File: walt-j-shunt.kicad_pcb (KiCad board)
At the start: 2 copper layers, 70 x 50 mm, 59 parts, among them J1 Screw_Terminal_01x03, Q1 NMOS, Q2 NJVMJD45H11T4G, Q3 PNP, Q4 NMOS, Q5 NJVMJD45H11T4G, Q6 PNP, U1 AD817, U2 AD817

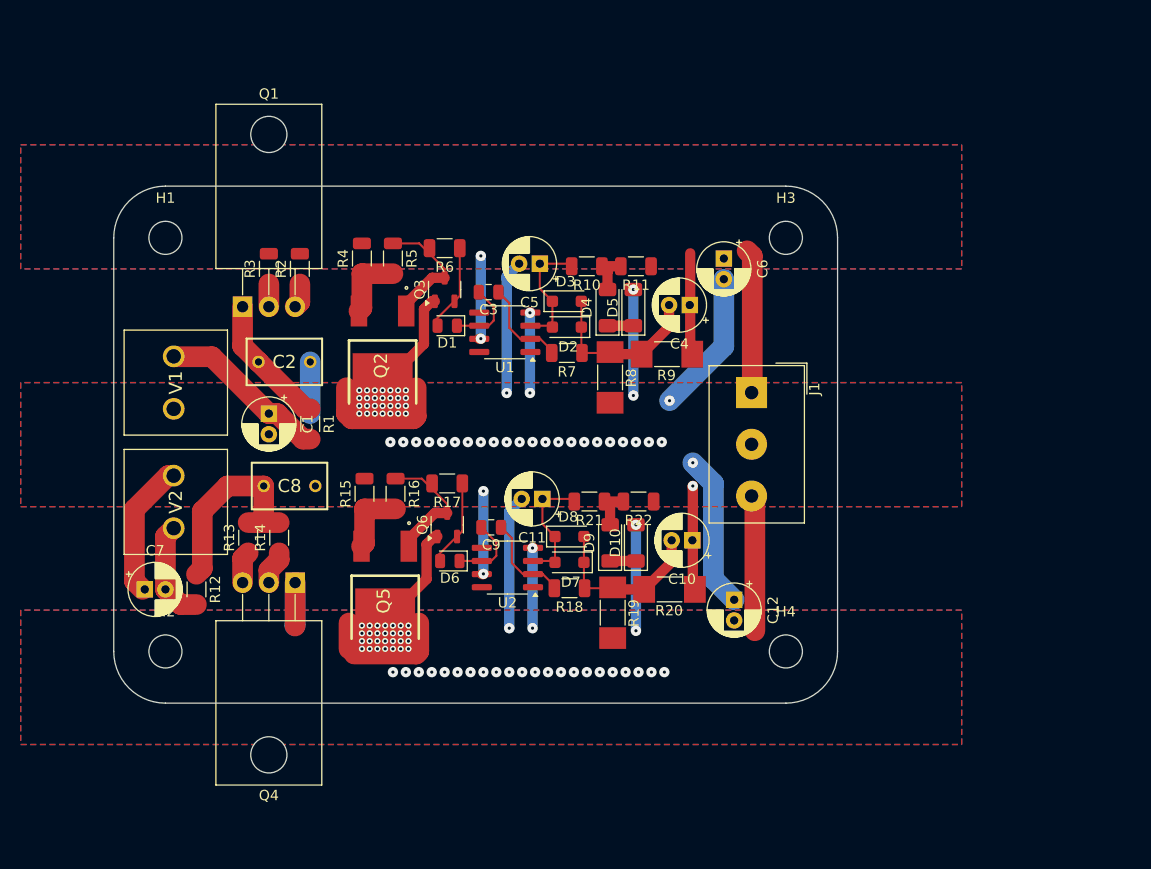
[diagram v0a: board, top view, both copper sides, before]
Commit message: Current design with SMD MOSFET (before switching to THT)
🤖 Generated with [Claude Code](https://claude.ai/code)

Co-Authored-By: Claude <noreply@anthropic.com>
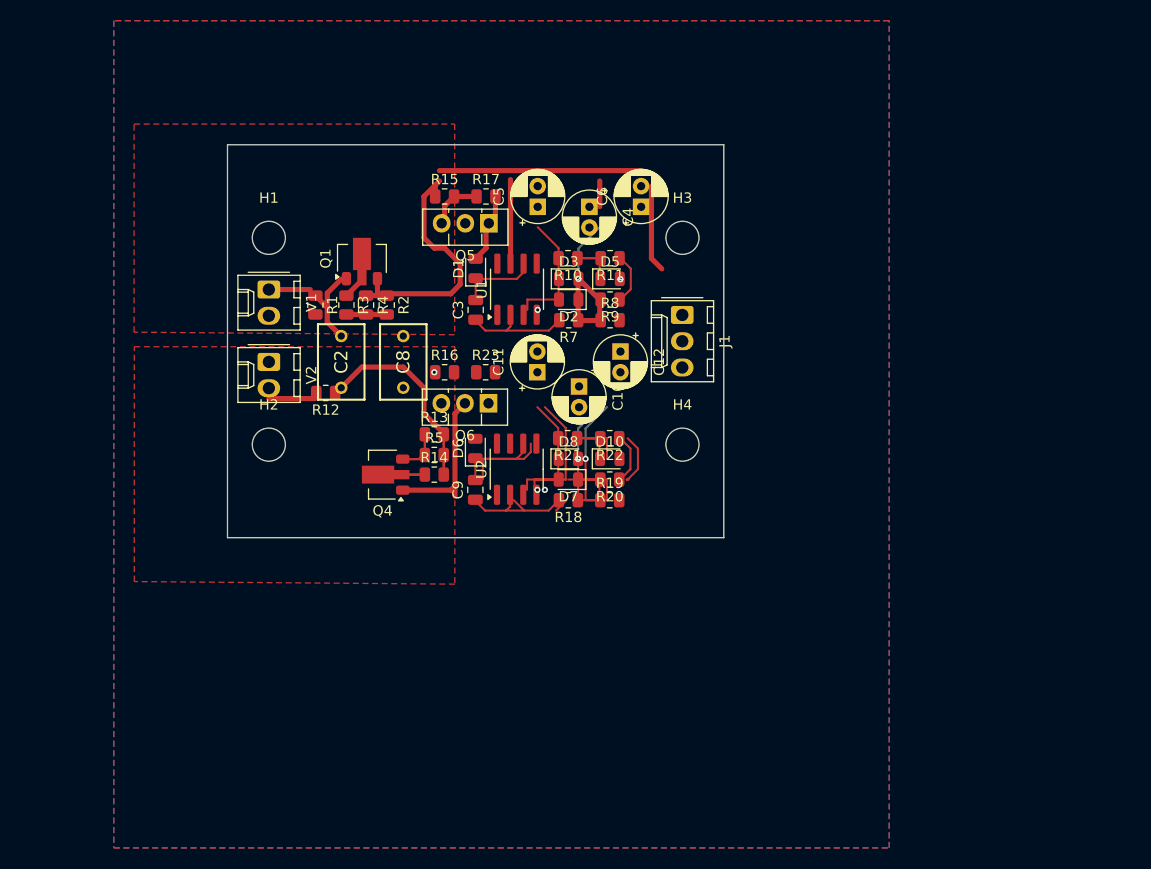
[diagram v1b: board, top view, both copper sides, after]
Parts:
- removed C1, C7: 120u, Capacitor_THT:CP_Radial_D5.0mm_P2.00mm
- removed D4, D9: D_Zener, Diode_SMD:D_MiniMELF
- removed Q2: NJVMJD45H11T4G, Samacsys:DPAK_(SINGLE-GAUGE)_TO-252(369C)_ISSUE_F
- removed Q3: PNP, Package_TO_SOT_SMD:SOT-23-3
- removed R6: 221r, Resistor_SMD:R_1206_3216Metric
- added R23: 440r, Resistor_SMD:R_0805_2012Metric, F.Cu at (131.0, 73.0)
- D10, D5: footprint Diode_SMD:D_MiniMELF -> Diode_SMD:D_0805_2012Metric
- D2, D3, D7, D8: footprint Diode_SMD:D_SOD-123F -> Diode_SMD:D_0805_2012Metric
- J1: footprint TerminalBlock_Altech:Altech_AK100_1x03_P5.00mm -> Connector_Molex:Molex_KK-254_AE-6410-03A_1x03_P2.54mm_Vertical
- Q1, Q4: footprint Package_TO_SOT_THT:TO-220-3_Horizontal_TabDown -> Package_TO_SOT_SMD:SOT-89-3
- Q5: value NJVMJD45H11T4G -> BD680; footprint Samacsys:DPAK_(SINGLE-GAUGE)_TO-252(369C)_ISSUE_F -> Package_TO_SOT_THT:TO-126-3_Vertical
- Q6: value PNP -> BD680; footprint Package_TO_SOT_SMD:SOT-23-3 -> Package_TO_SOT_THT:TO-126-3_Vertical
- R1, R10, R11, R12, R14, R15, R18, R21, R22, R3, R7: footprint Resistor_SMD:R_1206_3216Metric -> Resistor_SMD:R_0805_2012Metric
- R13, R2: value 5r -> 20r; footprint Resistor_SMD:R_1206_3216Metric -> Resistor_SMD:R_0805_2012Metric
- R16: value 49.9r -> 1r; footprint Resistor_SMD:R_1206_3216Metric -> Resistor_SMD:R_0805_2012Metric
- R17: value 221r -> 440r; footprint Resistor_SMD:R_1206_3216Metric -> Resistor_SMD:R_0805_2012Metric
- R19, R20, R8, R9: footprint Resistor_SMD:R_MELF_MMB-0207 -> Resistor_SMD:R_0805_2012Metric
- R4: value 1r -> 20r; footprint Resistor_SMD:R_1206_3216Metric -> Resistor_SMD:R_0805_2012Metric
- R5: value 49.9r -> 20r; footprint Resistor_SMD:R_1206_3216Metric -> Resistor_SMD:R_0805_2012Metric
- V1, V2: footprint Samacsys:395443002 -> Connector_Molex:Molex_KK-254_AE-6410-02A_1x02_P2.54mm_Vertical
- moved Q5 41.4 mm to (131.3, 58.6), turned to 180 degrees
- moved R15 29.8 mm to (127.0, 56.0), turned to 0 degrees
- moved Q4 29.2 mm to (121.0, 82.9)
- moved R17 28.0 mm to (131.0, 56.0), turned to 0 degrees
- moved C12 26.4 mm to (144.0, 71.0)
- moved R12 22.7 mm to (115.5, 75.0), turned to 180 degrees
- moved H2 22.4 mm to (110.0, 80.0)
- moved H4 22.4 mm to (150.0, 80.0)
- moved R13 20.6 mm to (126.0, 79.0), turned to 0 degrees
- moved R5 19.4 mm to (126.0, 81.0), turned to 0 degrees
- moved C10 18.5 mm to (140.0, 74.4), turned to -90 degrees
- moved C8 16.8 mm to (123.0, 69.5), turned to -90 degrees
- moved R14 16.2 mm to (126.0, 82.9), turned to 0 degrees
- moved Q1 15.0 mm to (119.0, 62.0), turned to 90 degrees
- moved V2 14.3 mm to (110.0, 72.0)
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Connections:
- net Net-(Q1-G) renamed /current_source/m_g
- net Net-(Q4-G) renamed /current_source1/m_g
- D5 pad 1: Net-(D4-K) -> Net-(D5-K)
- Q5 pad 1: Net-(Q6-E) -> Net-(D1-A)
- Q5 pad 2: Net-(Q5-Pad2) -> GND
- Q5 pad 3: neg_reg_out -> Net-(Q5-E)
- Q6 pad 1: neg_reg_out -> Net-(D6-A)
- Q6 pad 2: Net-(D6-A) -> neg_reg_out
- R10 pad 1: Net-(D4-A) -> Net-(D5-K)
- R11 pad 2: Net-(D4-A) -> Net-(D5-K)
- R15 pad 1: Net-(Q5-Pad2) -> pos_reg_out
- R15 pad 2: GND -> Net-(Q5-E)
- R16 pad 1: Net-(Q6-E) -> GND
- R16 pad 2: Net-(Q5-Pad2) -> Net-(Q6-E)
- R17 pad 1: Net-(D6-A) -> Net-(Q5-E)
- R17 pad 2: Net-(Q6-E) -> Net-(D1-A)
- R21 pad 1: Net-(D9-A) -> Net-(D10-K)
- R22 pad 2: Net-(D9-A) -> Net-(D10-K)
- R4 pad 1: Net-(Q2-Pad2) -> Net-(Q1-S)
- R5 pad 1: Net-(Q3-E) -> Net-(Q4-S)
- R5 pad 2: Net-(Q2-Pad2) -> /current_source1/plus
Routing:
- net GND: track 121.6 -> 10.2 mm, vias 60 -> 3
- net neg_reg_out: track 76.6 -> 14.6 mm, vias 55 -> 2
- net pos_reg_out: track 32.1 -> 68.9 mm, vias 2 -> 0
- net Net-(D7-K): track 17.2 -> 33.9 mm, vias 0 -> 2
- net Net-(Q6-E): track 12.3 -> 0.00 mm
- net Net-(Q3-E): track 12.3 -> 0.00 mm
- net bank-plus: track 16.5 -> 4.71 mm
- net Net-(D7-A): track 12.1 -> 23.8 mm
- net Net-(D10-K): track 2.50 -> 12.2 mm
- net Net-(D6-K): track 7.37 -> 15.5 mm
- net Net-(D6-A): track 8.01 -> 0.00 mm
- net Net-(Q2-Pad2): track 6.73 -> 0.00 mm
- net Net-(Q5-Pad2): track 6.73 -> 0.00 mm
- net Net-(D5-K): track 0.00 -> 6.09 mm
- net Net-(Q4-S): track 3.10 -> 8.79 mm
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- added copper zone on F.Cu, net /current_source/m_g
- added copper zone on F.Cu, net /current_source1/m_g
- removed copper zone on B.Cu, net neg_reg_out
- removed copper zone on F.Cu, net neg_reg_out
- removed copper zone on B.Cu, net pos_reg_out
- removed copper zone on F.Cu, net pos_reg_out
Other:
- board size 70 x 50 mm -> 48 x 38 mm

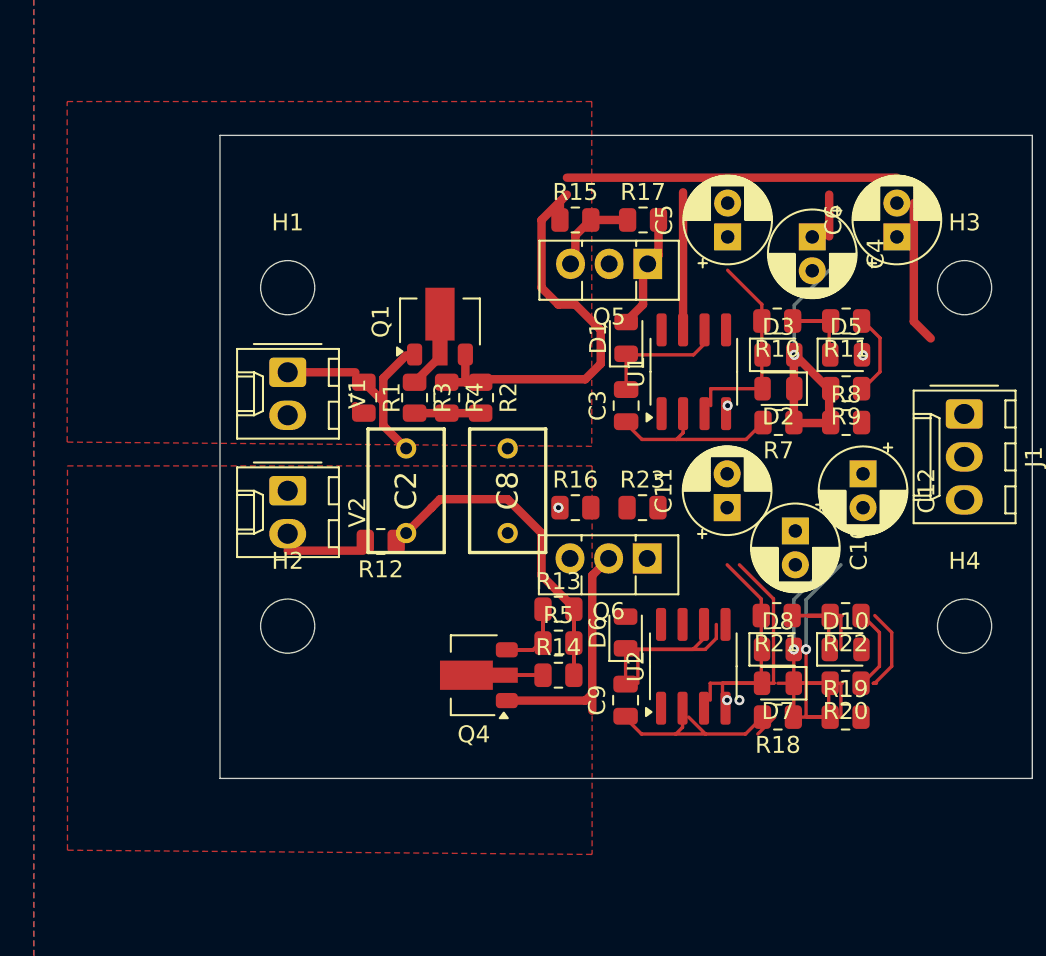
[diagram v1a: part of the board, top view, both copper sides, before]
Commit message: Switch to THT MOSFET - need to verify pinout, rough but closer
🤖 Generated with [Claude Code](https://claude.ai/code)

Co-Authored-By: Claude <noreply@anthropic.com>
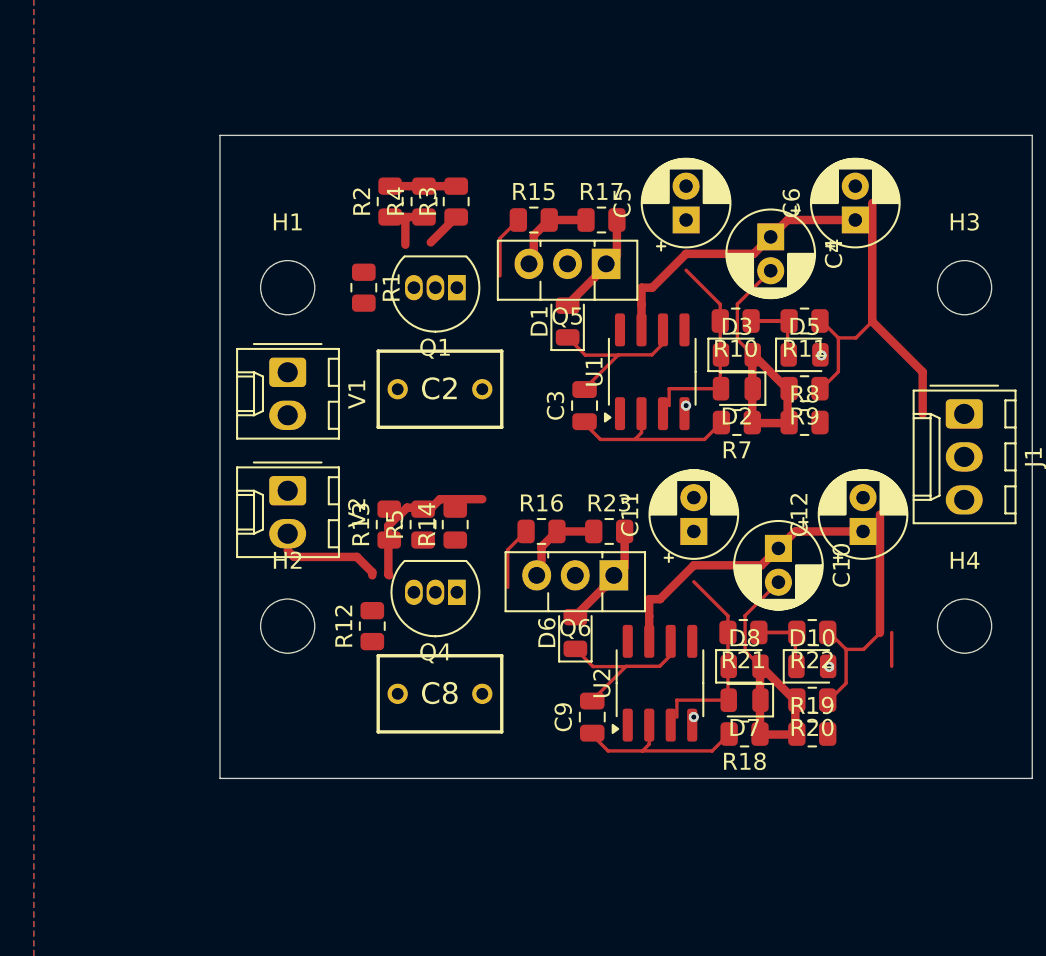
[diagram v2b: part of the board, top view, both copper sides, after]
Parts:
- Q1, Q4: footprint Package_TO_SOT_SMD:SOT-89-3 -> Package_TO_SOT_THT:TO-92_Inline
- moved C8 14.6 mm to (121.5, 84.0), turned to 180 degrees
- moved R2 12.8 mm to (116.1, 54.9), turned to 90 degrees
- moved R3 11.8 mm to (120.0, 54.9), turned to 90 degrees
- moved R4 11.7 mm to (118.1, 54.9), turned to 90 degrees
- moved R13 11.2 mm to (116.0, 74.0), turned to 90 degrees
- moved R14 10.8 mm to (119.9, 74.0), turned to 90 degrees
- moved R5 10.6 mm to (118.0, 74.0), turned to 90 degrees
- moved R1 6.50 mm to (114.5, 60.0)
- moved R12 5.02 mm to (115.0, 80.0), turned to 90 degrees
- moved Q4 5.00 mm to (120.0, 78.0)
- moved D1 3.59 mm to (126.5, 62.0)
- moved C2 3.54 mm to (116.5, 66.0), turned to 0 degrees
- moved C12 3.41 mm to (144.0, 74.4), turned to 90 degrees
- moved D6 2.97 mm to (127.0, 80.4)
- moved C5 2.65 mm to (133.5, 56.0)
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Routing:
- net GND: track 10.2 -> 37.0 mm, vias 3 -> 2
- net pos_reg_out: track 68.9 -> 45.8 mm
- net Net-(D7-K): track 33.9 -> 17.1 mm, vias 2 -> 0
- net /current_source1/plus: track 23.8 -> 9.16 mm
- net neg_reg_out: track 14.6 -> 0.00 mm
- net Net-(D7-A): track 23.8 -> 11.9 mm
- net Net-(Q4-S): track 8.79 -> 0.00 mm
- net pre-cur: track 8.25 -> 0.00 mm
- net Net-(D6-A): track 0.00 -> 6.21 mm
- net /current_source1/m_g: track 6.18 -> 0.00 mm
- net Net-(D10-K): track 12.2 -> 6.09 mm
- net Net-(D6-K): track 15.5 -> 9.97 mm
- net Net-(Q6-E): track 0.00 -> 5.47 mm
- net bank-plus: track 4.71 -> 0.00 mm
- net Net-(U2--): track 13.5 -> 10.6 mm
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- removed copper zone on F.Cu, net /current_source/m_g
- removed copper zone on F.Cu, net /current_source1/m_g

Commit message: Half layout done
🤖 Generated with [Claude Code](https://claude.ai/code)

Co-Authored-By: Claude <noreply@anthropic.com>
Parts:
- removed C11, C12: 120u, Capacitor_THT:CP_Radial_D5.0mm_P2.00mm
- removed D10: D_Zener, Diode_SMD:D_0805_2012Metric
- removed the R12 at (115.0, 80.0)
- removed the R14 at (119.9, 74.0)
- removed the R5 at (118.0, 74.0)
- added C7: 33pf, Capacitor_SMD:C_0805_2012Metric, F.Cu at (166.6, 96.9)
- added D4: gled, LED_SMD:LED_0805_2012Metric, F.Cu at (145.5, 55.5)
- added Q2: D45H11G, Package_TO_SOT_THT:TO-220-3_Vertical, F.Cu at (134.5, 55.1)
- added Q3: MMBT2907AL, Package_TO_SOT_SMD:SOT-23-3, F.Cu at (131.0, 58.5)
- added Q7: MMBT2907AL, Package_TO_SOT_SMD:SOT-23-3, F.Cu at (160.3, 96.4)
- added Q8: ZTX951, Package_TO_SOT_THT:TO-92Flat, F.Cu at (170.3, 97.2)
- added R15: 20r, Resistor_SMD:R_0805_2012Metric, F.Cu at (184.6, 81.8)
- added R17: 100r, Resistor_SMD:R_0805_2012Metric, F.Cu at (184.6, 87.7)
- added R24: 1k, Resistor_SMD:R_0805_2012Metric, F.Cu at (175.4, 75.8)
- added R25: 150r, Resistor_SMD:R_0805_2012Metric, F.Cu at (175.4, 78.8)
- added R26: 1.8k, Resistor_SMD:R_0805_2012Metric, F.Cu at (175.4, 81.7)
- added R3: 20r, Resistor_SMD:R_0805_2012Metric, F.Cu at (116.5, 58.5)
- added R7: 50r, Resistor_SMD:R_0805_2012Metric, F.Cu at (127.0, 58.5)
- added V2: VSIN, Connector_Molex:Molex_KK-254_AE-6410-02A_1x02_P2.54mm_Vertical, F.Cu at (184.7, 95.1)
- C10, C4, C5, C6: value 120u -> 100uf
- C8: value 1uf -> 100uf; footprint Samacsys:B32529C105J -> Capacitor_THT:CP_Radial_D5.0mm_P2.00mm
- C9: value 33pf -> 100uf; footprint Capacitor_SMD:C_0805_2012Metric -> Capacitor_THT:CP_Radial_D5.0mm_P2.00mm
- D1: value LED -> rled
- D5: value D_Zener -> rled
- D6: value LED -> D
- D8: value D -> gled; footprint Diode_SMD:D_0805_2012Metric -> LED_SMD:LED_0805_2012Metric
- Q1: value NMOS -> DN2540; footprint Package_TO_SOT_THT:TO-92_Inline -> Package_TO_SOT_THT:TO-220-3_Vertical
- Q4: value NMOS -> ZTX951; footprint Package_TO_SOT_THT:TO-92_Inline -> Package_TO_SOT_THT:TO-92Flat
- Q5: value BD680 -> DN2540; footprint Package_TO_SOT_THT:TO-126-3_Vertical -> Package_TO_SOT_THT:TO-220-3_Vertical
- Q6: value BD680 -> D45H11G; footprint Package_TO_SOT_THT:TO-126-3_Vertical -> Package_TO_SOT_THT:TO-220-3_Vertical
- R10: renamed from R8; value 1k -> 500r
- R11: renamed from R9; value 800r -> 2k
- R13: value 20r -> 150r
- R14: renamed from R11; value 1.82k -> 1.8k
- R16: value 1r -> 20r
- R18: value 499 -> 1r
- R19: value 1k -> 50r
- R2: value 20r -> 1r
- R20: value 800r -> 221r
- R21: value 1k -> 475
- R22: value 1.82k -> 500r
- R23: value 440r -> 2k
- R8: renamed from R17; value 440r -> 221r
- R9: renamed from R7; value 499 -> 475
- moved R2 82.3 mm to (184.6, 100.5), turned to 0 degrees
- moved R16 60.5 mm to (184.6, 84.8)
- moved Q5 60.1 mm to (185.6, 78.3), turned to 0 degrees
- moved R23 42.6 mm to (171.0, 81.7)
- moved U2 42.1 mm to (173.1, 92.5), turned to 0 degrees
- moved D6 40.3 mm to (166.6, 87.8), turned to 0 degrees
- moved C8 39.1 mm to (160.1, 77.6), turned to 0 degrees
- moved R21 34.4 mm to (171.0, 75.8), turned to 0 degrees
- moved D5 33.3 mm to (166.6, 84.7)
- moved R13 33.2 mm to (143.5, 55.5)
- moved Q4 32.2 mm to (141.2, 53.7), turned to -90 degrees
- moved C9 32.1 mm to (160.1, 84.2), turned to 0 degrees
- moved D8 31.8 mm to (166.6, 93.9)
- moved R18 31.4 mm to (166.6, 75.8), turned to 0 degrees
- moved D7 30.3 mm to (166.6, 90.8), turned to 0 degrees
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- renumbered C2 to C1, R10 to R12, R3 to R5, R15 to R6
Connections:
- C10 pad 2: Net-(D7-K) -> neg_reg_out
- C8 pad 2: /current_source1/plus -> Net-(D6-K)
- C9 pad 1: Net-(U2--) -> Net-(D6-A)
- C9 pad 2: Net-(D6-K) -> neg_reg_out
- D5 pad 2: GND -> Net-(D5-A)
- D7 pad 1: Net-(D7-K) -> Net-(D6-A)
- D7 pad 2: Net-(D7-A) -> Net-(D6-K)
- D8 pad 1: Net-(D7-A) -> neg_reg_out
- D8 pad 2: Net-(D7-K) -> Net-(D8-A)
- Q4 pad 1: neg_reg_out -> GND
- Q4 pad 2: /current_source1/m_g -> Net-(D4-A)
- Q4 pad 3: Net-(Q4-S) -> /reg/v-ref
- Q5 pad 1: Net-(D1-A) -> neg_reg_out
- Q5 pad 2: GND -> /current_source1/m_g
- Q5 pad 3: Net-(Q5-E) -> Net-(Q5-S)
- Q6 pad 1: Net-(D6-A) -> Net-(Q6-B)
- R12 pad 1: Net-(D5-K) -> /reg/v-ref
- R13 pad 1: Net-(Q4-S) -> /reg/v-ref
- R13 pad 2: /current_source1/plus -> Net-(D4-A)
- R14 pad 2: Net-(D5-K) -> /reg/v-ref
- R16 pad 1: GND -> Net-(Q5-S)
- R16 pad 2: Net-(Q6-E) -> /current_source1/+
- R18 pad 1: Net-(D7-K) -> GND
- R18 pad 2: Net-(U2--) -> Net-(Q6-E)
- R19 pad 1: Net-(D7-K) -> Net-(Q6-E)
- R19 pad 2: neg_reg_out -> Net-(Q6-B)
- R2 pad 1: Net-(Q1-S) -> /current_source1/+
- R2 pad 2: pos_reg_out -> Net-(R2-Pad2)
- R20 pad 1: GND -> Net-(Q6-B)
- R20 pad 2: Net-(D7-K) -> Net-(D5-A)
- R21 pad 1: Net-(D10-K) -> Net-(D6-K)
- R21 pad 2: Net-(D7-A) -> Net-(U2--)
- R22 pad 1: GND -> Net-(D6-K)
- R22 pad 2: Net-(D10-K) -> neg_reg_out
- R23 pad 1: Net-(Q6-E) -> GND
- R23 pad 2: Net-(D6-A) -> Net-(D6-K)
- R6 pad 2: Net-(Q5-E) -> Net-(Q2-E)
- R8 pad 1: Net-(Q5-E) -> Net-(Q2-B)
- U1 pad 1: unconnected-(U1-NULL-Pad1) -> Net-(D2-A)
- U1 pad 3: Net-(D2-A) -> pos_reg_out
- U1 pad 5: unconnected-(U1-NC-Pad5) -> Net-(D1-K)
- U1 pad 6: Net-(D1-K) -> (no net)
- U1 pad 7: pos_reg_out -> (no net)
- U1 pad 8: unconnected-(U1-NULL-Pad8) -> (no net)
- U2 pad 1: unconnected-(U2-NULL-Pad1) -> Net-(D6-A)
- U2 pad 3: Net-(D7-A) -> GND
- U2 pad 5: unconnected-(U2-NC-Pad5) -> Net-(D5-K)
- U2 pad 6: Net-(D6-K) -> (no net)
- U2 pad 7: GND -> (no net)
- U2 pad 8: unconnected-(U2-NULL-Pad8) -> (no net)
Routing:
- net GND: track 37.0 -> 0.00 mm, vias 2 -> 3
- net Net-(D7-K): track 17.1 -> 0.00 mm
- net pre-cur: track 0.00 -> 16.5 mm
- net pos_reg_out: track 45.8 -> 60.9 mm
- net /reg/v-ref: track 0.00 -> 13.0 mm
- net Net-(D7-A): track 11.9 -> 0.00 mm
- net Net-(D2-A): track 11.9 -> 22.6 mm
- net Net-(Q2-B): track 0.00 -> 10.7 mm
- net Net-(U2--): track 10.6 -> 0.00 mm
- net Net-(D6-K): track 9.97 -> 0.00 mm
- net /current_source1/plus: track 9.16 -> 0.00 mm
- net Net-(D6-A): track 6.21 -> 0.00 mm
- net Net-(D5-K): track 6.09 -> 0.00 mm
- net Net-(D10-K): track 6.09 -> 0.00 mm
- net Net-(R12-Pad2): track 5.71 -> 0.00 mm
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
